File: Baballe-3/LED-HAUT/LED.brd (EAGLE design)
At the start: 46.2 x 46.2 mm, 24 parts, among them Q1 200mA/50V, Q2 200mA/50V, Q3 200mA/50V, Q4 200mA/50V

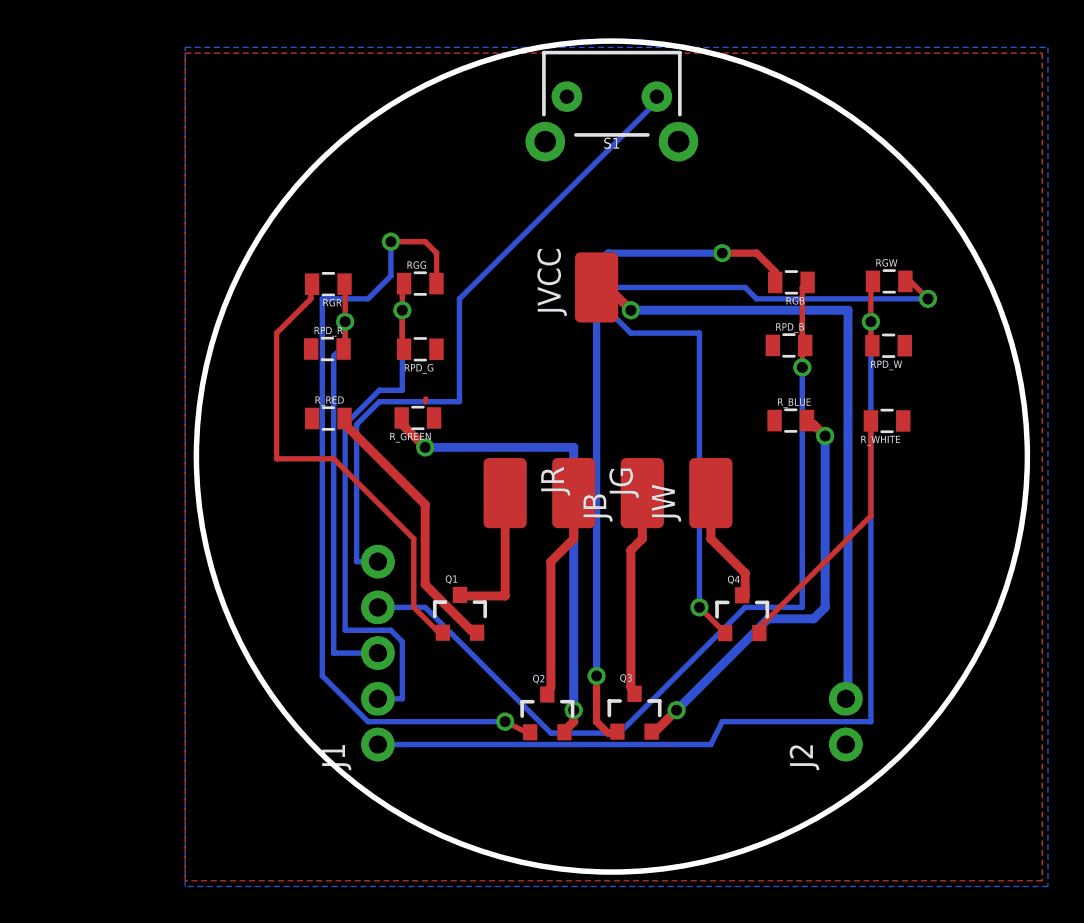
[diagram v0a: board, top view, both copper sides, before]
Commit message: Patch height error
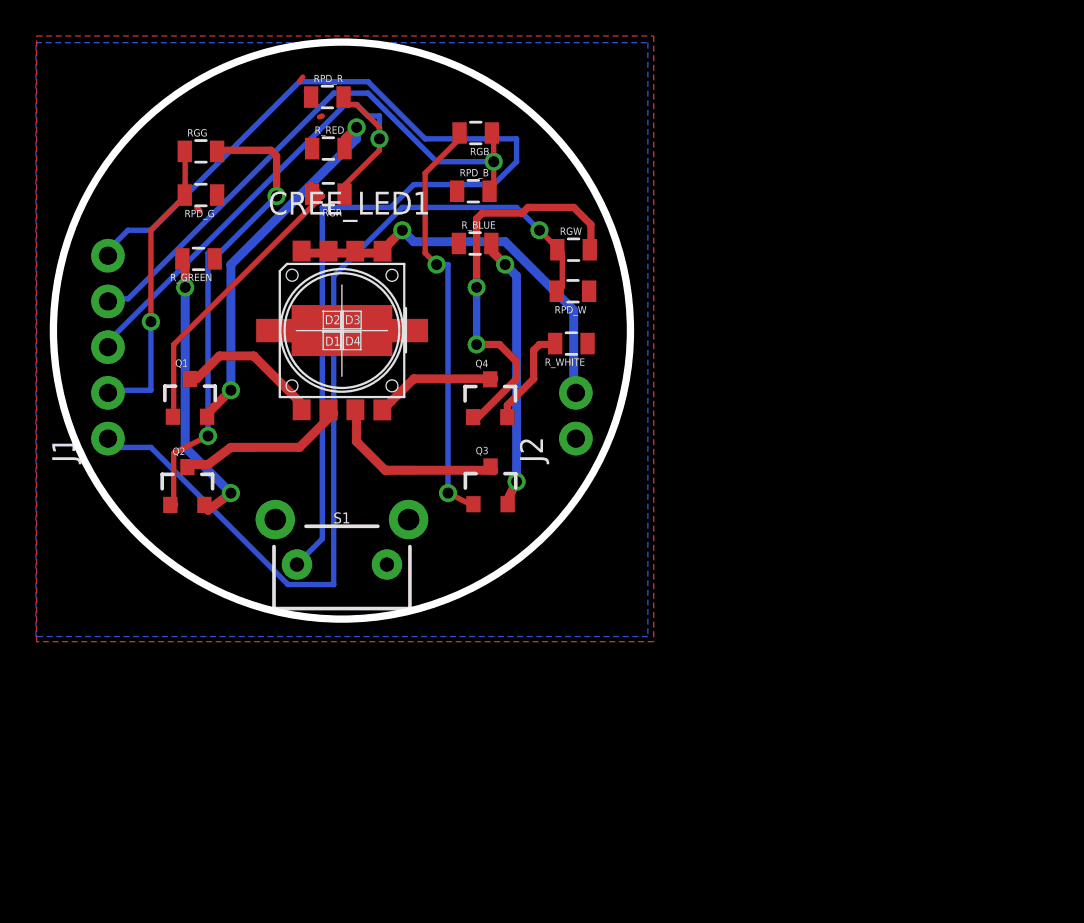
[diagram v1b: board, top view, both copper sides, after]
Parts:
- removed JB, JG, JR, JVCC, JW: (no value), SparkFun-Connectors:LUXEON-PAD
- added CREE_LED1: CREE_XL_MCE, CreeXL-MC-E:CREE_XL_MCE
- moved S1 30.0 mm to (43.0, 10.0), turned to 0 degrees
- moved Q2 23.7 mm to (34.4, 14.3)
- moved J1 22.7 mm to (30.0, 17.0)
- moved J2 22.7 mm to (56.0, 17.0)
- moved R_BLUE 20.1 mm to (50.4, 27.8)
- moved RPD_B 19.5 mm to (50.3, 30.7)
- moved RGB 19.4 mm to (50.4, 34.0)
- moved Q1 19.2 mm to (34.6, 19.2)
- moved Q4 18.4 mm to (51.2, 19.2)
- moved R_WHITE 18.1 mm to (55.7, 22.3)
- moved RPD_W 17.8 mm to (55.8, 25.2)
- moved RGW 17.6 mm to (55.9, 27.5)
- moved R_GREEN 15.1 mm to (35.0, 27.0)
- moved R_RED 15.0 mm to (42.2, 33.1)
- moved Q3 15.0 mm to (51.3, 14.4)
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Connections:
- net N$10: now also CREE_LED1.8; no longer JR.P$1
- net N$11: now also CREE_LED1.7; no longer JG.P$1
- net N$14: now also CREE_LED1.5; no longer JW.P$1
- net N$9: now also CREE_LED1.6; no longer JB.P$1
- net VCC: now also CREE_LED1.1, CREE_LED1.2, CREE_LED1.3, CREE_LED1.4; no longer JVCC.P$1
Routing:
- net O_BP: track 36.5 -> 61.9 mm
- net N$13: track 44.3 -> 22.3 mm
- net N$4: track 44.7 -> 26.2 mm
- net O_BLUE: track 47.7 -> 31.1 mm
- net O_GREEN: track 32.0 -> 16.5 mm
- net N$6: track 38.2 -> 23.3 mm
- net VCC: track 36.2 -> 22.6 mm
- net N$2: track 26.7 -> 16.0 mm
- net N$5: track 26.0 -> 17.1 mm
- net N$8: track 14.5 -> 5.67 mm
- net N$1: track 23.4 -> 15.3 mm
- net N$3: track 15.0 -> 20.9 mm, vias 0 -> 2
- net O_RED: track 24.8 -> 29.9 mm
- net O_WHITE: track 54.8 -> 50.7 mm
- net N$11: track 11.8 -> 9.64 mm
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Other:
- board size 46.2 x 46.2 mm -> 32.1 x 32.1 mm
